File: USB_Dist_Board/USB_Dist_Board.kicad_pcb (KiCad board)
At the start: 2 copper layers, 73 x 60 mm, 57 parts, among them P1 CONN_02X04, P2 CONN_01X03, P3 CONN_01X03, P5 CONN_01X04, P6 CONN_01X04, P7 CONN_02X04, Q1 BSS84, Q3 BSS84, SW1 RESET, SW2 BOOT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

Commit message: Main Board incomplete routing
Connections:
- P1 pad 2: /USB_D_GND -> (no net)
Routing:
- net /USB_D_GND: track 38.2 -> 35.5 mm
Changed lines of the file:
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@@
 (kicad_pcb (version 4) (host pcbnew 4.0.4-stable)
   (general
-    (links 155)
+    (links 154)
     (no_connects 0)
     (area 63.424999 67.924999 136.575001 128.035623)
     (thickness 1.6)
     (drawings 15)
-    (tracks 437)
+    (tracks 436)
     (zones 0)
     (modules 57)
@@
     (pad 1 thru_hole rect (at 0 0 270) (size 1.7272 1.7272) (drill 1.016) (layers *.Cu *.Mask)
       (net 36 /USB_D_GND))
-    (pad 2 thru_hole oval (at 0 2.54 270) (size 1.7272 1.7272) (drill 1.016) (layers *.Cu *.Mask)
-      (net 36 /USB_D_GND))
+    (pad 2 thru_hole oval (at 0 2.54 270) (size 1.7272 1.7272) (drill 1.016) (layers *.Cu *.Mask))
     (pad 3 thru_hole oval (at 2.54 0 270) (size 1.7272 1.7272) (drill 1.016) (layers *.Cu *.Mask)
       (net 11 /PWM1))
@@
   (segment (start 102.5 113.905) (end 102.5 125) (width 0.5) (layer B.Cu) (net 35))
   (segment (start 102.5 125) (end 102 125.5) (width 0.5) (layer B.Cu) (net 35))
+  (segment (start 128.5 85.54) (end 128.5 82.5) (width 0.5) (layer F.Cu) (net 36))
+  (segment (start 128.5 82.5) (end 129 82) (width 0.5) (layer F.Cu) (net 36))
+  (via (at 129 82) (size 0.6) (drill 0.4) (layers F.Cu B.Cu) (net 36))
   (segment (start 95.25 98) (end 95.25 97.25) (width 0.25) (layer B.Cu) (net 36))
   (via (at 95.25 97.25) (size 0.6) (drill 0.4) (layers F.Cu B.Cu) (net 36))
@@
   (segment (start 94.55 99.45) (end 95.25 98.75) (width 0.25) (layer B.Cu) (net 36))
   (via (at 95.25 98.75) (size 0.6) (drill 0.4) (layers F.Cu B.Cu) (net 36))
-  (segment (start 128.5 85.54) (end 125.96 85.54) (width 1) (layer F.Cu) (net 36))
-  (segment (start 123.54 85.54) (end 122.5 84.5) (width 0.25) (layer B.Cu) (net 36))
-  (via (at 122.5 84.5) (size 0.6) (drill 0.4) (layers F.Cu B.Cu) (net 36))
-  (segment (start 125.96 85.54) (end 123.54 85.54) (width 0.25) (layer B.Cu) (net 36))
   (segment (start 110.05 96.3) (end 110.05 97.55) (width 0.25) (layer B.Cu) (net 36))
   (segment (start 110.05 97.55) (end 110.5 98) (width 0.25) (layer B.Cu) (net 36))

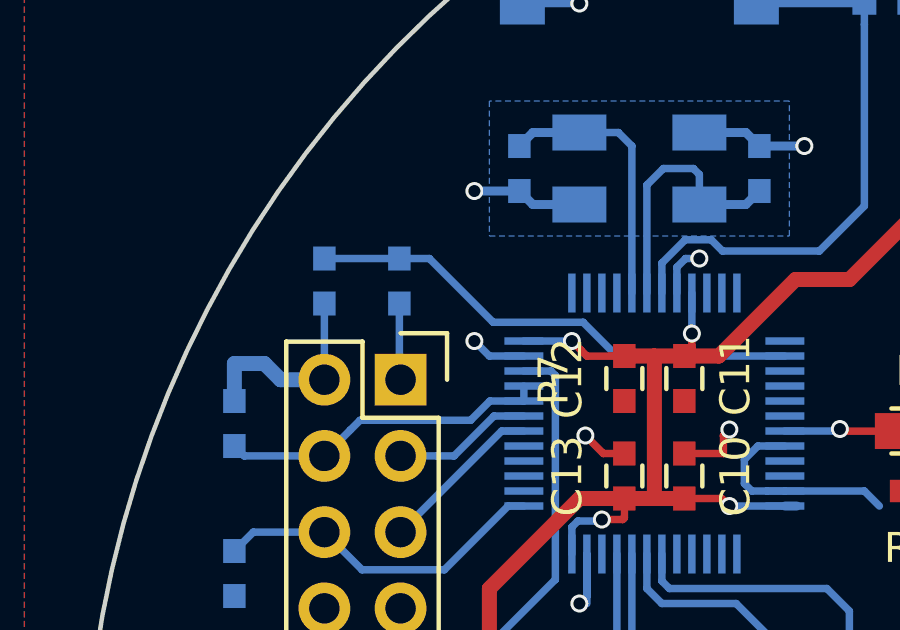
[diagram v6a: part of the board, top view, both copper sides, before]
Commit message: Main Board : Recover LED driver USB Dist Board : Delete ADC voltage divider
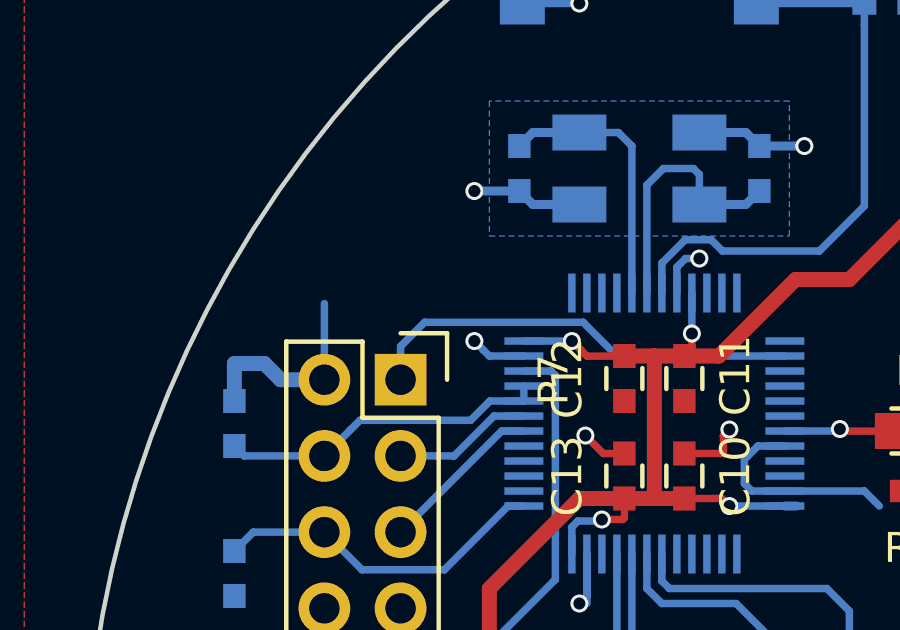
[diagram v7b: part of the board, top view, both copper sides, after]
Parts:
- removed R1, R2: R, Capacitors_SMD:C_0603
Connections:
- P7 pad 1: Net-(P7-Pad1) -> /ADC1
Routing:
- net Net-(P7-Pad1): track 2.56 -> 0.00 mm
- net /ADC1: track 16.7 -> 14.8 mm
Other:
- net class Default: trace_width 0.5 -> 0.25
